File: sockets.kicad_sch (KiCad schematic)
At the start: 8 parts

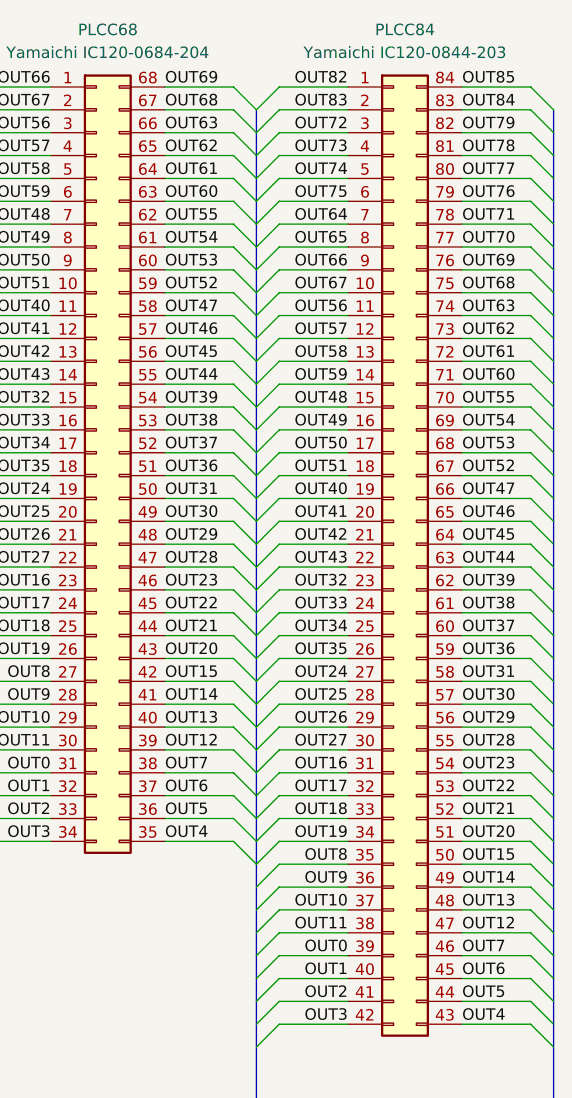
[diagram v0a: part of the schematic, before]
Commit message: update symbols and footprints with latest kicad
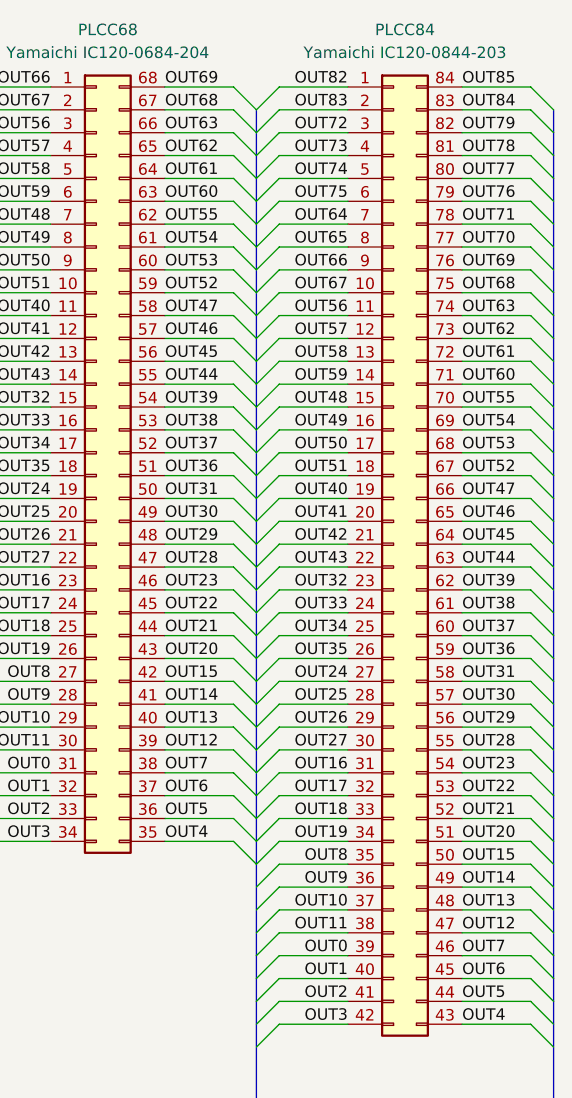
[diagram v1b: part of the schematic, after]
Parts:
- removed PLCC84: Yamaichi IC120-0844-203, Package_LCC:PLCC-84_THT-Socket, symbol Connector_Generic:Conn_02x42_Row_Letter_First
- added PLCC84: Yamaichi IC120-0844-203, Package_LCC:PLCC-84_THT-Socket, symbol Connector_Generic:Conn_02x40_Counter_Clockwise
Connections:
- net OUT0: now also PLCC84.39 (Pin_39)
- net OUT1: now also PLCC84.40 (Pin_40)
- net OUT10: now also PLCC84.37 (Pin_37)
- net OUT11: now also PLCC84.38 (Pin_38)
- net OUT12: now also PLCC84.47 (Pin_47)
- net OUT13: now also PLCC84.48 (Pin_48)
- net OUT14: now also PLCC84.49 (Pin_49)
- net OUT15: now also PLCC84.50 (Pin_50)
- net OUT16: now also PLCC84.31 (Pin_31)
- net OUT17: now also PLCC84.32 (Pin_32)
- net OUT18: now also PLCC84.33 (Pin_33)
- net OUT19: now also PLCC84.34 (Pin_34)
- net OUT2: now also PLCC84.41 (Pin_41)
- net OUT20: now also PLCC84.51 (Pin_51)
- net OUT21: now also PLCC84.52 (Pin_52)
- net OUT22: now also PLCC84.53 (Pin_53)
- net OUT23: now also PLCC84.54 (Pin_54)
- net OUT24: now also PLCC84.27 (Pin_27)
- net OUT25: now also PLCC84.28 (Pin_28)
- net OUT26: now also PLCC84.29 (Pin_29)
- net OUT27: now also PLCC84.30 (Pin_30)
- net OUT28: now also PLCC84.55 (Pin_55)
- net OUT29: now also PLCC84.56 (Pin_56)
- net OUT3: now also PLCC84.42 (Pin_42)
- net OUT30: now also PLCC84.57 (Pin_57)
- net OUT31: now also PLCC84.58 (Pin_58)
- net OUT32: now also PLCC84.23 (Pin_23)
- net OUT33: now also PLCC84.24 (Pin_24)
- net OUT34: now also PLCC84.25 (Pin_25)
- net OUT35: now also PLCC84.26 (Pin_26)
- net OUT36: now also PLCC84.59 (Pin_59)
- net OUT37: now also PLCC84.60 (Pin_60)
- net OUT38: now also PLCC84.61 (Pin_61)
- net OUT39: now also PLCC84.62 (Pin_62)
- net OUT4: now also PLCC84.43 (Pin_43)
- net OUT40: now also PLCC84.19 (Pin_19)
- net OUT41: now also PLCC84.20 (Pin_20)
- net OUT42: now also PLCC84.21 (Pin_21)
- net OUT43: now also PLCC84.22 (Pin_22)
- net OUT44: now also PLCC84.63 (Pin_63)
- net OUT45: now also PLCC84.64 (Pin_64)
- net OUT46: now also PLCC84.65 (Pin_65)
- net OUT47: now also PLCC84.66 (Pin_66)
- net OUT48: now also PLCC84.15 (Pin_15)
- net OUT49: now also PLCC84.16 (Pin_16)
- net OUT5: now also PLCC84.44 (Pin_44)
- net OUT50: now also PLCC84.17 (Pin_17)
- net OUT51: now also PLCC84.18 (Pin_18)
- net OUT52: now also PLCC84.67 (Pin_67)
- net OUT53: now also PLCC84.68 (Pin_68)
- net OUT54: now also PLCC84.69 (Pin_69)
- net OUT55: now also PLCC84.70 (Pin_70)
- net OUT56: now also PLCC84.11 (Pin_11)
- net OUT57: now also PLCC84.12 (Pin_12)
- net OUT58: now also PLCC84.13 (Pin_13)
- net OUT59: now also PLCC84.14 (Pin_14)
- net OUT6: now also PLCC84.45 (Pin_45)
- net OUT60: now also PLCC84.71 (Pin_71)
- net OUT61: now also PLCC84.72 (Pin_72)
- net OUT62: now also PLCC84.73 (Pin_73)
- net OUT63: now also PLCC84.74 (Pin_74)
- net OUT64: now also PLCC84.7 (Pin_7)
- net OUT65: now also PLCC84.8 (Pin_8)
- net OUT66: now also PLCC84.9 (Pin_9)
- net OUT67: now also PLCC84.10 (Pin_10)
- net OUT68: now also PLCC84.75 (Pin_75)
- net OUT69: now also PLCC84.76 (Pin_76)
- net OUT7: now also PLCC84.46 (Pin_46)
- net OUT70: now also PLCC84.77 (Pin_77)
- net OUT71: now also PLCC84.78 (Pin_78)
- net OUT72: now also PLCC84.3 (Pin_3)
- net OUT73: now also PLCC84.4 (Pin_4)
- net OUT74: now also PLCC84.5 (Pin_5)
- net OUT75: now also PLCC84.6 (Pin_6)
- net OUT76: now also PLCC84.79 (Pin_79)
- net OUT77: now also PLCC84.80 (Pin_80)
- net OUT78: now also PLCC84.81 (Pin_81)
- net OUT79: now also PLCC84.82 (Pin_82)
- net OUT8: now also PLCC84.35 (Pin_35)
- net OUT82: now also PLCC84.1 (Pin_1)
- net OUT83: now also PLCC84.2 (Pin_2)
- net OUT84: now also PLCC84.83 (Pin_83)
- net OUT85: now also PLCC84.84 (Pin_84)
- net OUT9: now also PLCC84.36 (Pin_36)
